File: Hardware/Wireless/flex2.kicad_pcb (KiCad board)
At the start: 2 copper layers, 17.6 x 9.4 mm, 2 parts

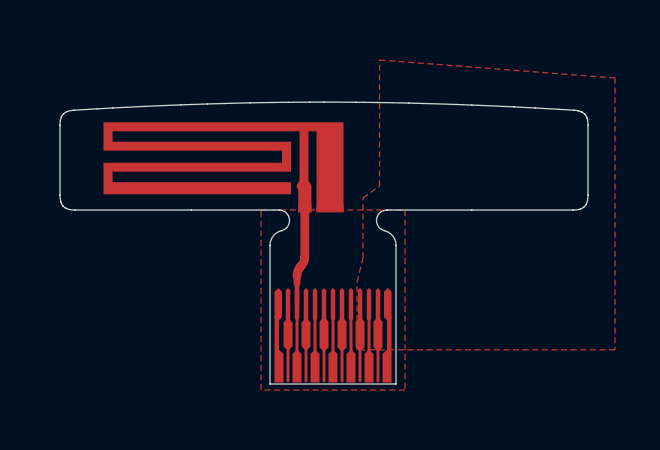
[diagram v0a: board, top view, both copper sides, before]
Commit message: added gyro, flex pcb antenna
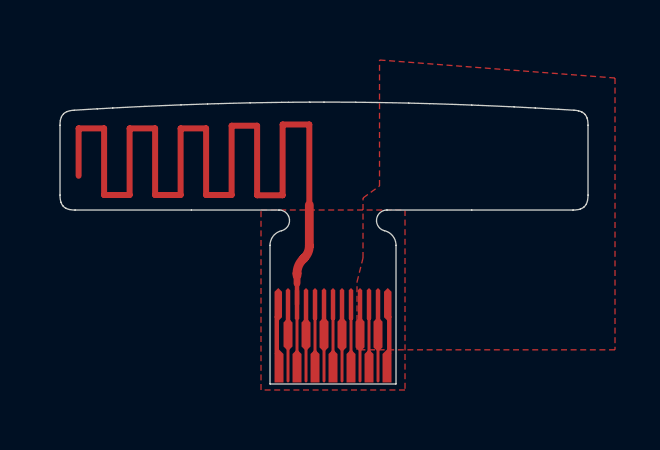
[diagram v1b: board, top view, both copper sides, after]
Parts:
- removed the REF** at (176.4, 88.3)
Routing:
- net antenna: track 3.41 -> 33.5 mm

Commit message: new flex and new pcbs
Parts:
- added AE**: 2.4GHz-meander-antenna, Library:2.4GHz-meander-antenna, F.Cu at (173.0, 78.0)
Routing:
- net antenna: track 33.5 -> 14.9 mm
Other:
- board size 17.6 x 9.4 mm -> 32.4 x 39.6 mm
